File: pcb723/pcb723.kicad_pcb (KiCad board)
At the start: 4 copper layers, 12 parts, among them U1 STM32H723ZGT6

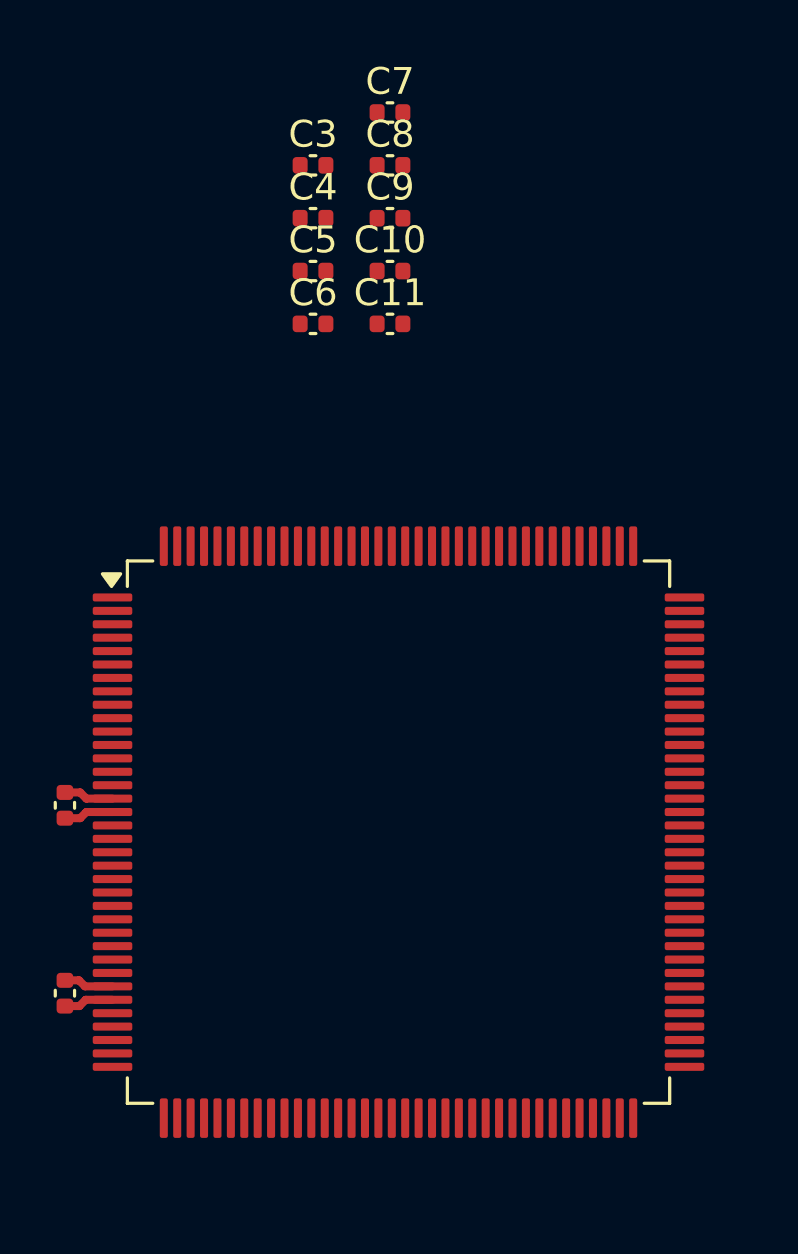
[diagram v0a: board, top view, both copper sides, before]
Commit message: Place 100nF capacitors
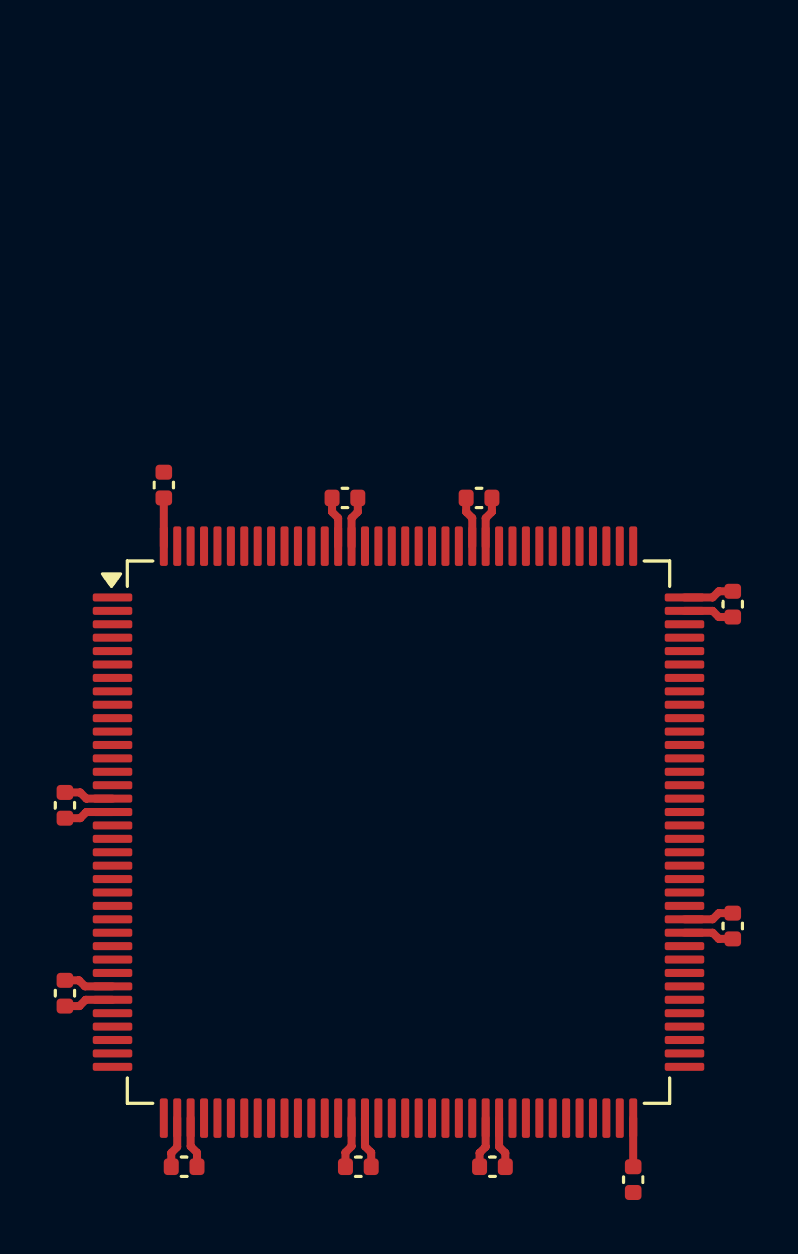
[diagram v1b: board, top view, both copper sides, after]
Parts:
- moved C3 37.6 mm to (118.8, 91.2)
- moved C4 35.4 mm to (125.3, 91.2)
- moved C6 34.1 mm to (135.6, 91.7), turned to 90 degrees
- moved C5 34.1 mm to (130.3, 91.2)
- moved C7 32.9 mm to (139.3, 82.2), turned to 90 degrees
- moved C8 20.8 mm to (139.3, 70.2), turned to 90 degrees
- moved C9 10.9 mm to (129.8, 66.3), turned to 180 degrees
- moved C11 10.4 mm to (118.1, 65.8), turned to -90 degrees
- moved C10 8.63 mm to (124.8, 66.3), turned to 180 degrees
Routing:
- net +3V3: track 3.74 -> 20.7 mm
- net GND: track 3.74 -> 17.0 mm

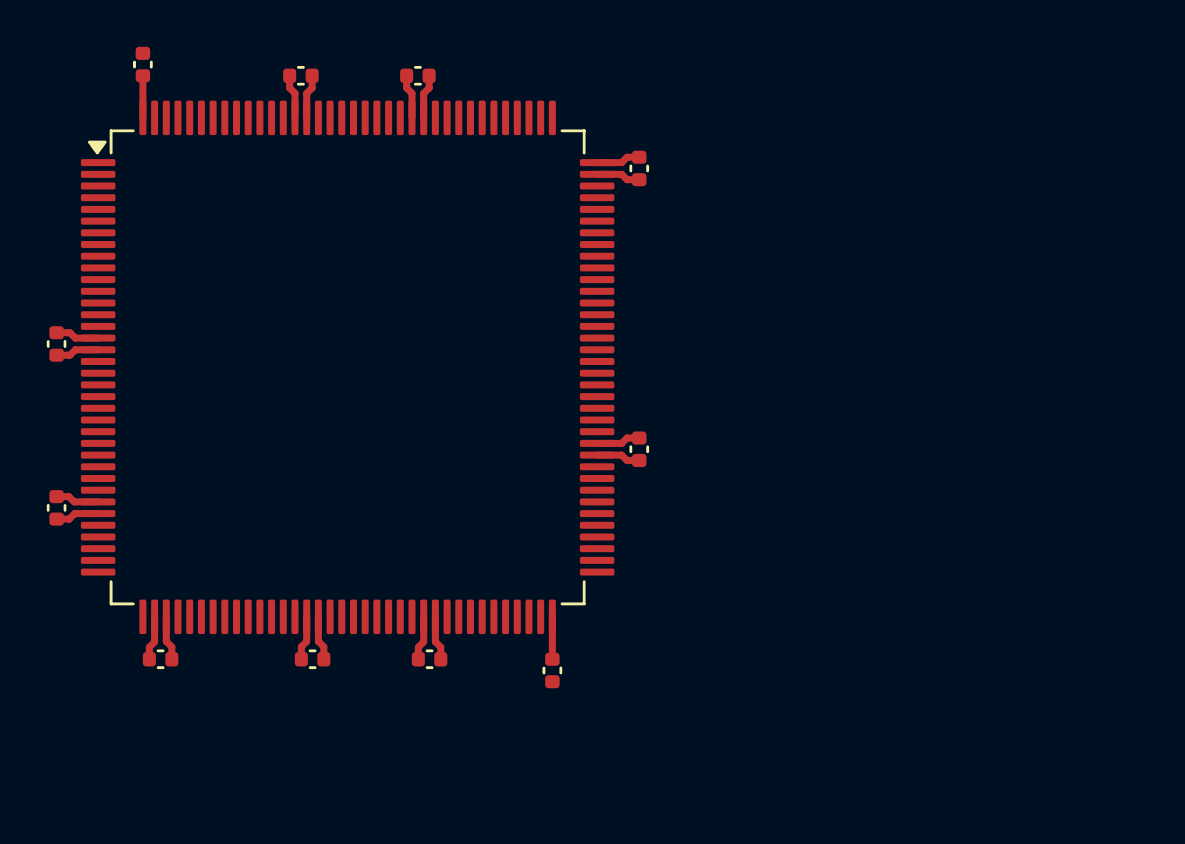
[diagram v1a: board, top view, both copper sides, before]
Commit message: Add jumpers
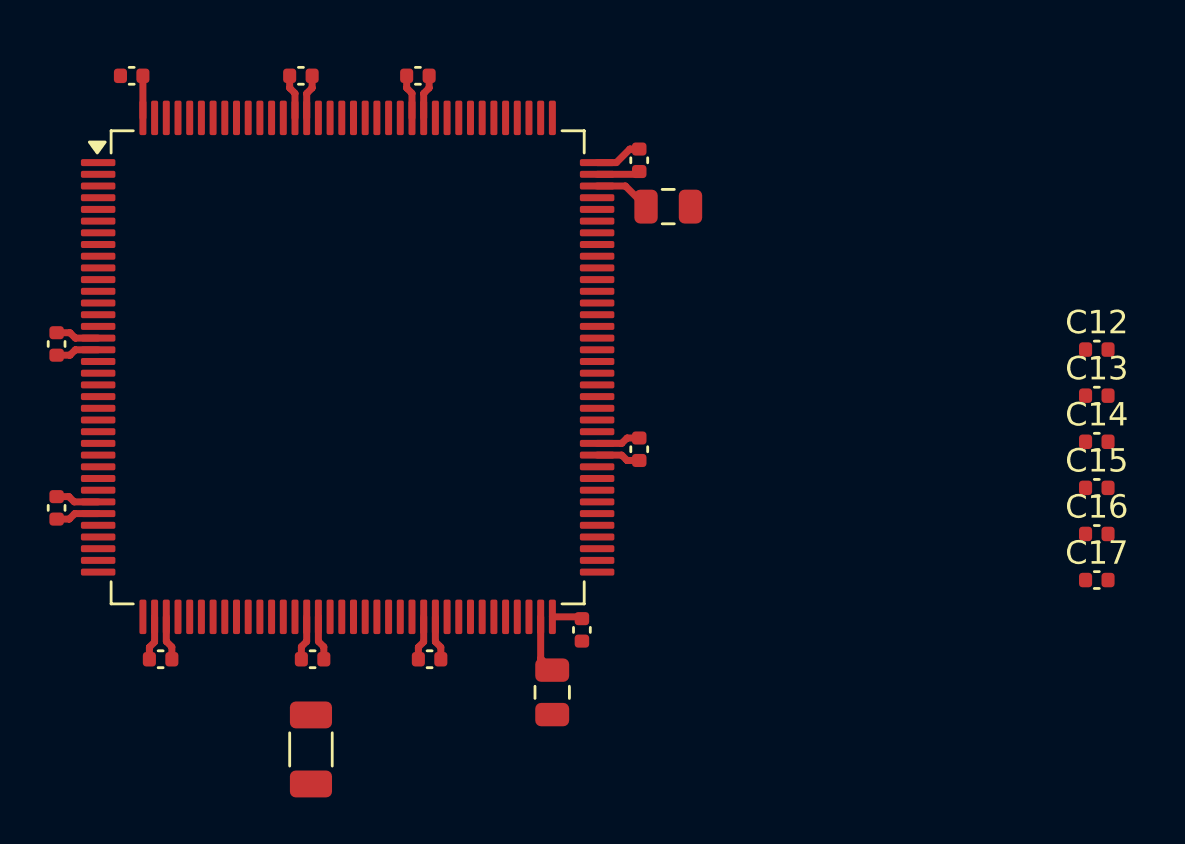
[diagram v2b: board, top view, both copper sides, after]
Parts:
- added C12: 1u, Capacitor_SMD:C_0402_1005Metric, F.Cu at (158.9, 78.0)
- added C13: 1u, Capacitor_SMD:C_0402_1005Metric, F.Cu at (158.9, 80.0)
- added C14: 1u, Capacitor_SMD:C_0402_1005Metric, F.Cu at (158.9, 81.9)
- added C15: 100n, Capacitor_SMD:C_0402_1005Metric, F.Cu at (158.9, 83.9)
- added C16: 100n, Capacitor_SMD:C_0402_1005Metric, F.Cu at (158.9, 85.9)
- added C17: 1u, Capacitor_SMD:C_0402_1005Metric, F.Cu at (158.9, 87.8)
- added C18: 4u7, Capacitor_SMD:C_1206_3216Metric, F.Cu at (125.3, 95.1)
- added C19: 2u2, Capacitor_SMD:C_0805_2012Metric, F.Cu at (140.5, 71.9)
- added C20: 2u2, Capacitor_SMD:C_0805_2012Metric, F.Cu at (135.6, 92.6)
- moved C6 2.15 mm to (136.8, 90.0)
- moved C11 0.68 mm to (117.6, 66.3), turned to 0 degrees
- moved C8 0.35 mm to (139.3, 69.9)
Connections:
- U1 pad 106: unconnected-(U1-VCAP-Pad106) -> Net-(C19-Pad2)
- U1 pad 138: unconnected-(U1-BOOT0-Pad138) -> /BOOT0
- U1 pad 143: unconnected-(U1-PDR_ON-Pad143) -> /PDR_ON
- U1 pad 23: unconnected-(U1-PH0-Pad23) -> /PH0
- U1 pad 24: unconnected-(U1-PH1-Pad24) -> /PH1
- U1 pad 25: unconnected-(U1-NRST-Pad25) -> /NRST
- U1 pad 32: unconnected-(U1-VREF+-Pad32) -> +3V3
- U1 pad 33: unconnected-(U1-VDDA-Pad33) -> +3V3
- U1 pad 6: unconnected-(U1-VBAT-Pad6) -> +3V3
- U1 pad 71: unconnected-(U1-VCAP-Pad71) -> Net-(C20-Pad2)
- U1 pad 95: unconnected-(U1-VDD33USB-Pad95) -> +3V3
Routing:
- net Net-(C20-Pad2): track 0.00 -> 2.48 mm
- net Net-(C19-Pad2): track 0.00 -> 2.45 mm

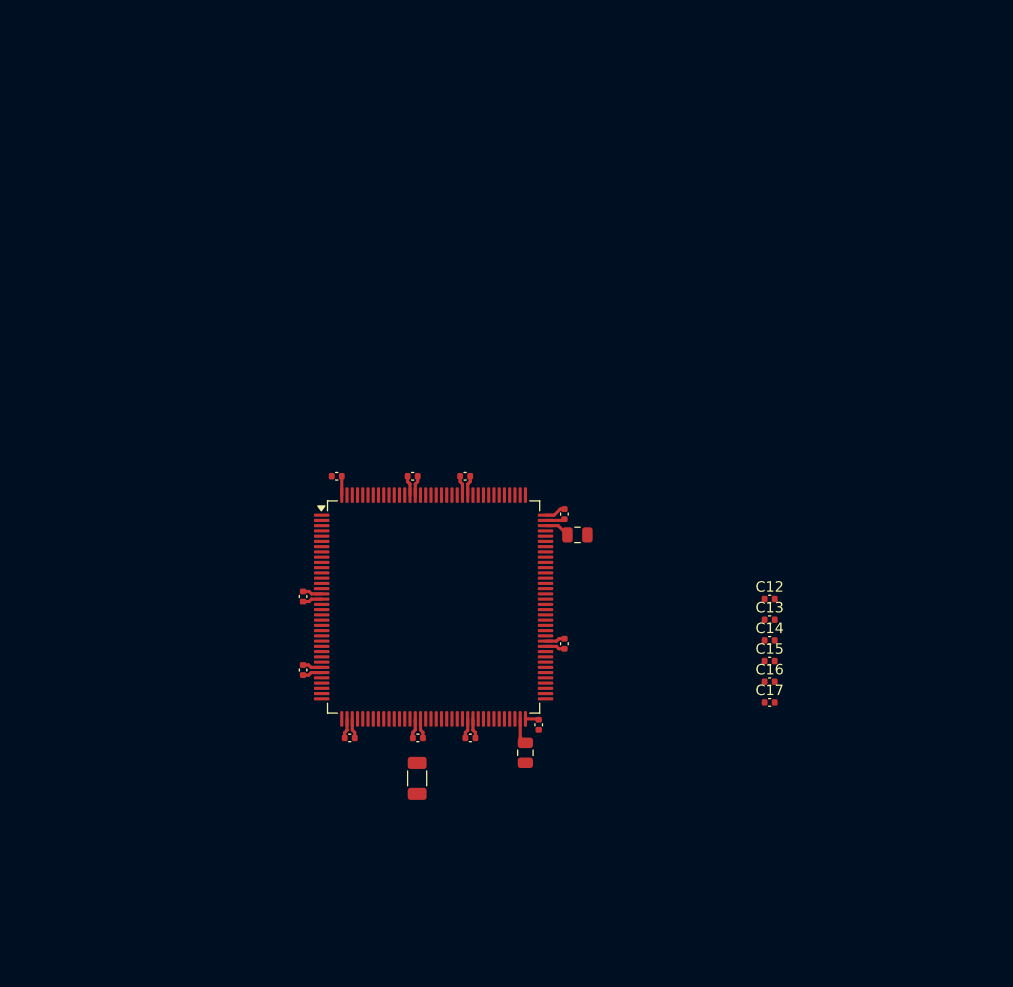
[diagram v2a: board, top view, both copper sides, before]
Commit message: Add ceramic crystal
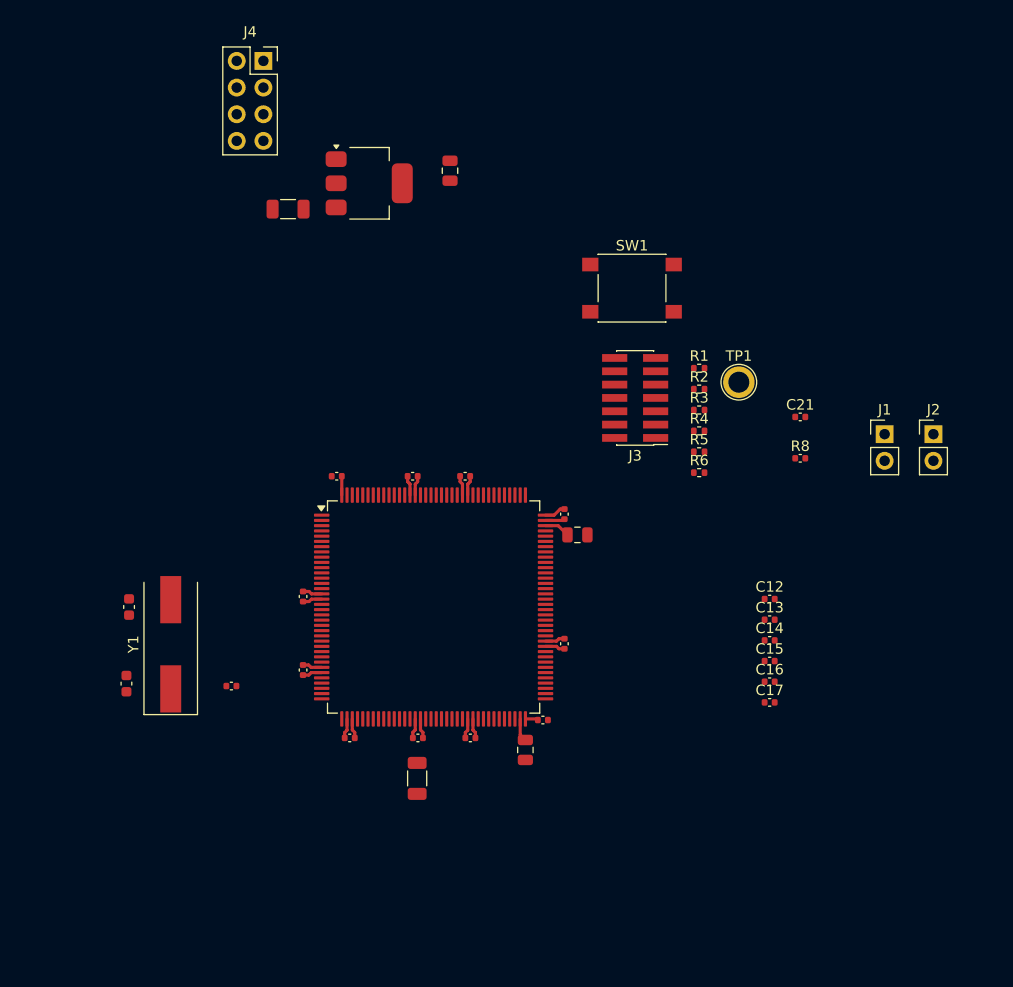
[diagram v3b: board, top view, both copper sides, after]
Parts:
- added C21: 1u, Capacitor_SMD:C_0402_1005Metric, F.Cu at (161.8, 60.6)
- added C22: 30p, Capacitor_SMD:C_0603_1608Metric, F.Cu at (97.6, 86.0)
- added C23: 30p, Capacitor_SMD:C_0603_1608Metric, F.Cu at (97.8, 78.8)
- added C24: 22u, Capacitor_SMD:C_0805_2012Metric, F.Cu at (128.4, 37.2)
- added C25: 10u, Capacitor_SMD:C_1206_3216Metric, F.Cu at (113.0, 40.8)
- added J1: Conn_01x02_Pin, Connector_PinHeader_2.54mm:PinHeader_1x02_P2.54mm_Vertical, F.Cu at (169.8, 62.3)
- added J2: Conn_01x02_Pin, Connector_PinHeader_2.54mm:PinHeader_1x02_P2.54mm_Vertical, F.Cu at (174.5, 62.3)
- added J3: Conn_02x07_Odd_Even, Connector_PinHeader_1.27mm:PinHeader_2x07_P1.27mm_Vertical_SMD, F.Cu at (146.0, 58.8)
- added J4: Conn_02x04_Odd_Even, Connector_PinSocket_2.54mm:PinSocket_2x04_P2.54mm_Vertical, F.Cu at (110.6, 26.7)
- added R1: 10k, Resistor_SMD:R_0402_1005Metric, F.Cu at (152.1, 56.0)
- added R2: 100R, Resistor_SMD:R_0402_1005Metric, F.Cu at (152.1, 58.0)
- added R3: 100R, Resistor_SMD:R_0402_1005Metric, F.Cu at (152.1, 60.0)
- added R4: 10k, Resistor_SMD:R_0402_1005Metric, F.Cu at (152.1, 62.0)
- added R5: 10k, Resistor_SMD:R_0402_1005Metric, F.Cu at (152.1, 64.0)
- added R6: 100R, Resistor_SMD:R_0402_1005Metric, F.Cu at (152.1, 66.0)
- added R7: 33R, Capacitor_SMD:C_0402_1005Metric, F.Cu at (107.6, 86.3)
- added R8: 100R, Capacitor_SMD:C_0402_1005Metric, F.Cu at (161.8, 64.6)
- added SW1: SW_Push, Button_Switch_SMD:SW_Push_1P1T_NO_6x6mm_H9.5mm, F.Cu at (145.7, 48.4)
- added TP1: TestPoint, TestPoint:TestPoint_Plated_Hole_D2.0mm, F.Cu at (155.9, 57.3)
- added U2: AMS1117-3.3, Package_TO_SOT_SMD:SOT-223-3_TabPin2, F.Cu at (120.7, 38.4)
- added Y1: 8MHz 20pF, Crystal:Crystal_SMD_HC49-SD, F.Cu at (101.8, 82.3)
- moved C6 0.60 mm to (137.2, 89.5), turned to 180 degrees
- moved C20 0.27 mm to (135.6, 92.4)
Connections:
- U1 pad 103: unconnected-(U1-PA11-Pad103) -> /USB_FS_N
- U1 pad 104: unconnected-(U1-PA12-Pad104) -> /USB_FS_P
- U1 pad 105: unconnected-(U1-PA13(JTMS-Pad105) -> /T_SWDIO
- U1 pad 109: unconnected-(U1-PA14(JTCK-Pad109) -> /T_SWCLK
- U1 pad 110: unconnected-(U1-PA15(JTDI)-Pad110) -> /T_JTDI
- U1 pad 133: unconnected-(U1-PB3(JTDO-Pad133) -> /T_SWO
- U1 pad 136: unconnected-(U1-PB6-Pad136) -> /T_VCP_TX
- U1 pad 137: unconnected-(U1-PB7-Pad137) -> /T_VCP_RX
- U1 pad 25: /NRST -> /T_NRST

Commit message: Place decoupling capacitors
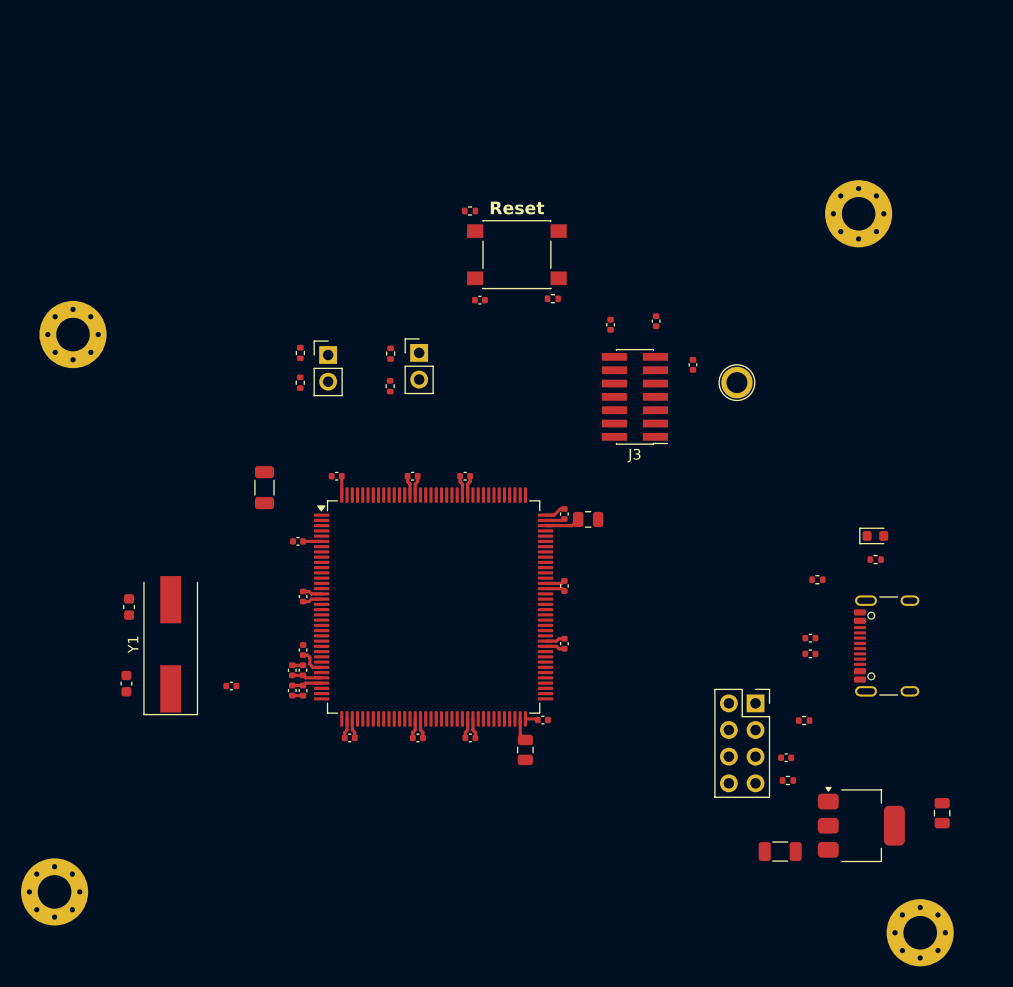
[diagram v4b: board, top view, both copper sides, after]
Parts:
- added C26: 100n, Capacitor_SMD:C_0402_1005Metric, F.Cu at (160.4, 93.1)
- added D1: LED, LED_SMD:LED_0603_1608Metric, F.Cu at (168.9, 72.0)
- added H1: MountingHole_Pad, MountingHole:MountingHole_3.2mm_M3_Pad_Via, F.Cu at (92.5, 52.8)
- added H2: MountingHole_Pad, MountingHole:MountingHole_3.2mm_M3_Pad_Via, F.Cu at (167.3, 41.3)
- added H3: MountingHole_Pad, MountingHole:MountingHole_3.2mm_M3_Pad_Via, F.Cu at (90.7, 105.9)
- added H4: MountingHole_Pad, MountingHole:MountingHole_3.2mm_M3_Pad_Via, F.Cu at (173.2, 109.8)
- added J5: USB_C_Receptacle_USB2.0_16P, Connector_USB:USB_C_Receptacle_GCT_USB4105-xx-A_16P_TopMnt_Horizontal, F.Cu at (171.1, 82.5)
- added R10: 100R, Capacitor_SMD:C_0402_1005Metric, F.Cu at (148.0, 51.5)
- added R11: 5k1, Resistor_SMD:R_0402_1005Metric, F.Cu at (162.1, 89.6)
- added R12: 5k1, Resistor_SMD:R_0402_1005Metric, F.Cu at (163.4, 76.2)
- added R13: 1k, Resistor_SMD:R_0402_1005Metric, F.Cu at (160.6, 95.3)
- added R14: 1k, Resistor_SMD:R_0402_1005Metric, F.Cu at (169.0, 74.2)
- added R15: 100R, Capacitor_SMD:C_0402_1005Metric, F.Cu at (162.7, 83.2)
- added R16: 100R, Capacitor_SMD:C_0402_1005Metric, F.Cu at (162.7, 81.7)
- added R9: 100R, Capacitor_SMD:C_0402_1005Metric, F.Cu at (143.7, 51.9)
- moved C25 77.1 mm to (159.9, 102.0)
- moved U2 77.1 mm to (167.6, 99.6)
- moved J4 77.1 mm to (157.5, 87.9)
- moved C24 77.1 mm to (175.3, 98.4)
- moved J2 58.2 mm to (116.8, 54.7)
- moved C14 45.7 mm to (113.4, 86.7), turned to 90 degrees
- moved C17 45.6 mm to (113.4, 84.8), turned to -90 degrees
- moved C12 45.3 mm to (113.9, 72.5)
- moved J1 45.0 mm to (125.5, 54.5)
- moved C15 44.5 mm to (114.4, 86.7), turned to 90 degrees
- moved C16 44.5 mm to (114.4, 84.8), turned to -90 degrees
- moved R4 38.7 mm to (114.1, 54.5), turned to -90 degrees
- moved R3 38.1 mm to (114.1, 57.4), turned to -90 degrees
- moved R6 33.1 mm to (130.3, 41.0), turned to 180 degrees
- moved C21 32.5 mm to (131.2, 49.5), turned to 180 degrees
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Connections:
- U1 pad 136: /T_VCP_TX -> Net-(U1-PB6)
- U1 pad 137: /T_VCP_RX -> Net-(U1-PB7)
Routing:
- net +3V3: track 20.2 -> 30.5 mm
- net GND: track 17.0 -> 19.1 mm
- net Net-(C19-Pad2): track 2.45 -> 3.35 mm
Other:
- board text added: "Reset"
